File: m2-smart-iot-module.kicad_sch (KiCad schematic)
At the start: 3 parts

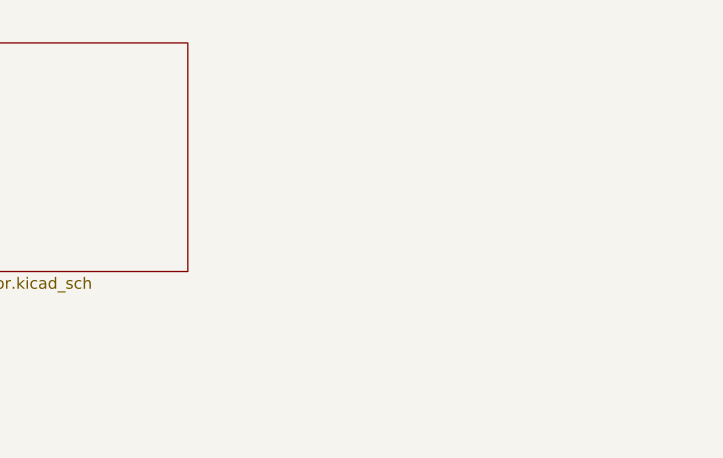
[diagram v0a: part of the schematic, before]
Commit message: Added FTDI schematic
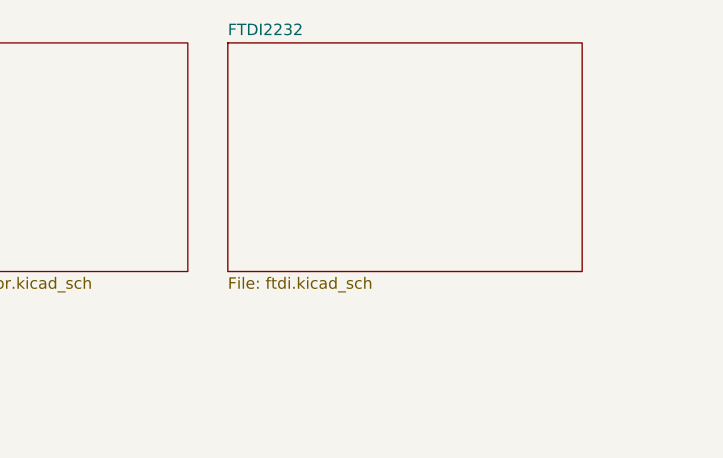
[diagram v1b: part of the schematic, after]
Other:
- added sheet FTDI2232 (ftdi.kicad_sch)
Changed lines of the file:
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@@
+    )
+  )
+  (sheet (at 328.93 114.3) (size 39.37 25.4) (fields_autoplaced)
+    (stroke (width 0.1524) (type solid) (color 0 0 0 0))
+    (fill (color 0 0 0 0.0000))
+    (property "Sheet name" "FTDI2232" (id 0) (at 328.93 113.5884 0)
+      (effects (font (size 1.27 1.27)) (justify left bottom))
+    )
+    (property "Sheet file" "ftdi.kicad_sch" (id 1) (at 328.93 140.2846 0)
+      (effects (font (size 1.27 1.27)) (justify left top))
     )
   )
@@
     (path "/00000000-0000-0000-0000-0000605233cc" (page "5"))
     (path "/00000000-0000-0000-0000-0000605198ab" (page "6"))
+    (path "/68410b93-aca6-44d3-bd1e-cd427080a29c" (page "7"))
   )
   (symbol_instances
@@
       (reference "#PWR0108") (unit 1) (value "GND") (footprint "")
     )
+    (path "/68410b93-aca6-44d3-bd1e-cd427080a29c/11afe054-5b39-465b-bea7-140a33a54372"
+      (reference "#PWR?") (unit 1) (value "GND") (footprint "")
+    )
+    (path "/68410b93-aca6-44d3-bd1e-cd427080a29c/1e138a19-c9d3-4ce1-abef-10dc6e03d6b0"
+      (reference "#PWR?") (unit 1) (value "GND") (footprint "")
+    )
+    (path "/68410b93-aca6-44d3-bd1e-cd427080a29c/3439d517-461f-421f-a266-6f812446a438"
+      (reference "#PWR?") (unit 1) (value "GND") (footprint "")
+    )
+    (path "/68410b93-aca6-44d3-bd1e-cd427080a29c/34daddf2-4aa9-45c0-a5dd-1378e6b328a3"
+      (reference "#PWR?") (unit 1) (value "GND") (footprint "")
+    )
+    (path "/68410b93-aca6-44d3-bd1e-cd427080a29c/41977174-5359-4b9f-993d-9e04af2325ce"
+      (reference "#PWR?") (unit 1) (value "GND") (footprint "")
+    )
+    (path "/68410b93-aca6-44d3-bd1e-cd427080a29c/5dd26dfc-010f-4b59-98a9-fc53bac77c22"
+      (reference "#PWR?") (unit 1) (value "GND") (footprint "")
+    )
+    (path "/68410b93-aca6-44d3-bd1e-cd427080a29c/81cfe2dd-64d2-49dc-92f1-faef74ed356b"
+      (reference "#PWR?") (unit 1) (value "GND") (footprint "")
+    )
+    (path "/68410b93-aca6-44d3-bd1e-cd427080a29c/852b28f0-6b74-43e6-8ae5-e14a61a04115"
+      (reference "#PWR?") (unit 1) (value "GND") (footprint "")
+    )
+    (path "/68410b93-aca6-44d3-bd1e-cd427080a29c/b1091a6c-2627-4ea9-977d-a02c6e01983d"
+      (reference "#PWR?") (unit 1) (value "GND") (footprint "")
+    )
+    (path "/68410b93-aca6-44d3-bd1e-cd427080a29c/b24ad7d7-7447-4ac2-a396-7e9974858242"
+      (reference "#PWR?") (unit 1) (value "GND") (footprint "")
+    )
+    (path "/68410b93-aca6-44d3-bd1e-cd427080a29c/e0a02e44-9724-4dcf-a201-9611e14adbdf"
+      (reference "#PWR?") (unit 1) (value "GND") (footprint "")
+    )
+    (path "/68410b93-aca6-44d3-bd1e-cd427080a29c/e6cb064a-7148-4e0a-bbed-942b0b8c1538"
+      (reference "#PWR?") (unit 1) (value "GND") (footprint "")
+    )
     (path "/00000000-0000-0000-0000-000060519809/00000000-0000-0000-0000-00006053cae5"
       (reference "ANT1") (unit 1) (value "ANT-2.45-CHP-T") (footprint "m2-smart-iot-module-footprints:Linx-ANT-2.45-CHP-T-MFG")
@@
       (reference "C77") (unit 1) (value "C_100n_0402") (footprint "m2-smart-iot-module-footprints:0402-cap")
     )
+    (path "/68410b93-aca6-44d3-bd1e-cd427080a29c/00128c11-9ae6-4452-9d40-6eed6ed4fa92"
+      (reference "C?") (unit 1) (value "C_100n_0402") (footprint "antmicro-footprints:0402-cap")
+    )
+    (path "/68410b93-aca6-44d3-bd1e-cd427080a29c/0683ecee-ab3f-4084-b163-cb6e41987b93"
+      (reference "C?") (unit 1) (value "C_100n_0402") (footprint "antmicro-footprints:0402-cap")
+    )
+    (path "/68410b93-aca6-44d3-bd1e-cd427080a29c/07656054-dac2-43ac-a0ba-60cc3622062b"
+      (reference "C?") (unit 1) (value "C_100n_0402") (footprint "antmicro-footprints:0402-cap")
+    )
+    (path "/68410b93-aca6-44d3-bd1e-cd427080a29c/1f05b071-c8f4-4c21-8c00-c3d2755cccf7"
+      (reference "C?") (unit 1) (value "C_100n_0402") (footprint "antmicro-footprints:0402-cap")
+    )
+    (path "/68410b93-aca6-44d3-bd1e-cd427080a29c/2d7a560d-7fde-4b37-b777-8fd058908345"
+      (reference "C?") (unit 1) (value "C_100n_0402") (footprint "antmicro-footprints:0402-cap")
+    )
+    (path "/68410b93-aca6-44d3-bd1e-cd427080a29c/315f3ffb-9d51-441d-9c46-0e9b7750238d"
+      (reference "C?") (unit 1) (value "C_18p_0402") (footprint "antmicro-footprints:0402-cap")
+    )
+    (path "/68410b93-aca6-44d3-bd1e-cd427080a29c/4143701c-d634-41bd-a301-0c60c388ad5f"
+      (reference "C?") (unit 1) (value "C_100n_0402") (footprint "antmicro-footprints:0402-cap")
+    )
+    (path "/68410b93-aca6-44d3-bd1e-cd427080a29c/73c959b5-8152-4fad-9ade-293313183a87"
+      (reference "C?") (unit 1) (value "C_18p_0402") (footprint "antmicro-footprints:0402-cap")
+    )
+    (path "/68410b93-aca6-44d3-bd1e-cd427080a29c/add7447d-93c8-4ac2-acdb-bb2a61238b8f"
+      (reference "C?") (unit 1) (value "C_10u_0805") (footprint "m2-smart-iot-module-footprints:0805-cap")
+    )
+    (path "/68410b93-aca6-44d3-bd1e-cd427080a29c/e69a35cc-c2a3-403f-b7de-acd2c8207974"
+      (reference "C?") (unit 1) (value "C_100n_0402") (footprint "antmicro-footprints:0402-cap")
+    )
     (path "/00000000-0000-0000-0000-000060519809/00000000-0000-0000-0000-0000623b8f1e"
       (reference "D1") (unit 1) (value "KP-1608CGCK") (footprint "m2-smart-iot-module-footprints:LED0603")
@@
       (reference "FB1") (unit 1) (value "BLM21PG600SN") (footprint "m2-smart-iot-module-footprints:0805-res")
     )
+    (path "/68410b93-aca6-44d3-bd1e-cd427080a29c/1ba44061-29ba-43cb-9cde-cc3db1725136"
+      (reference "FB?") (unit 1) (value "BLM21PG600SN") (footprint "m2-smart-iot-module-footprints:0805-res")
+    )
     (path "/00000000-0000-0000-0000-0000604cff57/659b3f22-a9f3-4d19-b979-88ffbed06828"
       (reference "IC1") (unit 1) (value "UPD720201K8-711-BAC-A") (footprint "antmicro-footprints:QFN40P800X800X90-69N-D")
@@
       (reference "R52") (unit 1) (value "R_0R_0402") (footprint "antmicro-footprints:0402-res")
     )
+    (path "/00000000-0000-0000-0000-0000605233cc/071ba9ef-8d4a-4032-8611-9e9457c33aa7"
+      (reference "R?") (unit 1) (value "R_1k_0402") (footprint "antmicro-footprints:0402-res")
+    )
+    (path "/68410b93-aca6-44d3-bd1e-cd427080a29c/22e4935e-cfb3-465f-b2e5-6b3ebcec47e9"
+      (reference "R?") (unit 1) (value "R_10k_0402") (footprint "antmicro-footprints:0402-res")
+    )
+    (path "/00000000-0000-0000-0000-000060519809/357517c7-91f3-4445-89df-5a4994fd51bb"
+      (reference "R?") (unit 1) (value "R_1k_0402") (footprint "antmicro-footprints:0402-res")
+    )
+    (path "/68410b93-aca6-44d3-bd1e-cd427080a29c/4691fe08-6cea-4c9e-9cc2-3894d30e602d"
+      (reference "R?") (unit 1) (value "R_10k_0402") (footprint "antmicro-footprints:0402-res")
+    )
+    (path "/68410b93-aca6-44d3-bd1e-cd427080a29c/5c795cc7-77ec-4acc-9612-76929e97dfd9"
+      (reference "R?") (unit 1) (value "R_2k2_0402") (footprint "antmicro-footprints:0402-res")
+    )
+    (path "/68410b93-aca6-44d3-bd1e-cd427080a29c/85e35e99-01ee-4c85-a0e8-9b9263b7c426"
+      (reference "R?") (unit 1) (value "R_10k_0402") (footprint "antmicro-footprints:0402-res")
+    )
+    (path "/68410b93-aca6-44d3-bd1e-cd427080a29c/a49e9949-2706-459a-b507-cea25a41afde"
+      (reference "R?") (unit 1) (value "R_12k_0402") (footprint "antmicro-footprints:0402-res")
+    )
+    (path "/68410b93-aca6-44d3-bd1e-cd427080a29c/e29c8173-da2a-43c0-8ce3-638aaee3ba36"
+      (reference "R?") (unit 1) (value "R_10k_0402") (footprint "antmicro-footprints:0402-res")
+    )
     (path "/00000000-0000-0000-0000-000060519809/00000000-0000-0000-0000-00006094bf1c"
       (reference "SW1") (unit 1) (value "PTS840_GK_SMTR_LFS") (footprint "m2-smart-iot-module-footprints:CK-PTS840_GK_SMTR_LFS-0")
@@
       (reference "TP28") (unit 1) (value "TP_SMD1MM") (footprint "m2-smart-iot-module-footprints:Testpoint_smd_1mm")
     )
+    (path "/68410b93-aca6-44d3-bd1e-cd427080a29c/3f5a84f7-9e18-4808-aab2-0e69509107a0"
+      (reference "U1") (unit 1) (value "FT2232H-56Q") (footprint "antmicro-footprints:QFN-56-1EP_8x8mm_P0.5mm_EP5.5.9x5.9mm")
+    )
     (path "/00000000-0000-0000-0000-0000604cff57/00000000-0000-0000-0000-0000604de031"
       (reference "U2") (unit 1) (value "SST25VF512A") (footprint "m2-smart-iot-module-footprints:SOIC8-SST25VF512A-33-4I-SAE-Level_B")
@@
       (reference "U10") (unit 1) (value "MIC2877-5.0YFT-TR") (footprint "m2-smart-iot-module-footprints:FTQFN")
     )
+    (path "/68410b93-aca6-44d3-bd1e-cd427080a29c/d41af900-20ce-4a2e-b28a-32b01b68e5cf"
+      (reference "U?") (unit 1) (value "93LC56CT-IMC") (footprint "antmicro-footprints:DFN-8_2x3mm")
+    )
     (path "/00000000-0000-0000-0000-0000604cff57/00000000-0000-0000-0000-00006060e650"
       (reference "Y1") (unit 1) (value "NX3225SA-24M") (footprint "m2-smart-iot-module-footprints:NDK-NX3225SA-0-0-MFG")
@@
       (reference "Y3") (unit 1) (value "ABS06-32.768KHZ-9-1-T") (footprint "m2-smart-iot-module-footprints:Abracon-ABS06-32.768KHZ-T-0")
     )
+    (path "/68410b93-aca6-44d3-bd1e-cd427080a29c/af6ea41f-d80e-49de-a9b5-51d22eadba5d"
+      (reference "Y?") (unit 1) (value "ABM8G-12M-18-D2Y-T") (footprint "antmicro-footprints:KX-7")
+    )
   )

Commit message: Bumped version to 1.2.2
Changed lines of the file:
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@@
     (title "M.2 Smart IoT Module")
     (date "2022-07-11")
-    (rev "1.2.1")
+    (rev "1.2.2")
     (comment 1 "www.antmicro.com")
     (comment 2 "Antmicro Ltd.")
@@
     )
   )
-  (sheet (at 158.75 114.3) (size 38.1 25.4) (fields_autoplaced)
+  (sheet (at 125.095 114.3) (size 38.1 25.4) (fields_autoplaced)
     (stroke (width 0) (type solid) (color 0 0 0 0))
     (fill (color 0 0 0 0.0000))
-    (property "Sheet name" "PCIe-USB-Bridge" (id 0) (at 158.75 113.5884 0)
+    (property "Sheet name" "PCIe-USB-Bridge" (id 0) (at 125.095 113.5884 0)
       (effects (font (size 1.27 1.27)) (justify left bottom))
     )
-    (property "Sheet file" "pcie-usb-bridge.kicad_sch" (id 1) (at 158.75 140.2846 0)
+    (property "Sheet file" "pcie-usb-bridge.kicad_sch" (id 1) (at 125.095 140.2846 0)
       (effects (font (size 1.27 1.27)) (justify left top))
     )
   )
-  (sheet (at 116.205 114.3) (size 38.1 25.4) (fields_autoplaced)
+  (sheet (at 82.55 114.3) (size 38.1 25.4) (fields_autoplaced)
     (stroke (width 0) (type solid) (color 0 0 0 0))
     (fill (color 0 0 0 0.0000))
-    (property "Sheet name" "M2-Pins" (id 0) (at 116.205 113.5884 0)
+    (property "Sheet name" "M2-Pins" (id 0) (at 82.55 113.5884 0)
       (effects (font (size 1.27 1.27)) (justify left bottom))
     )
-    (property "Sheet file" "M2-Pins.kicad_sch" (id 1) (at 116.205 140.2846 0)
+    (property "Sheet file" "M2-Pins.kicad_sch" (id 1) (at 82.55 140.2846 0)
       (effects (font (size 1.27 1.27)) (justify left top))
     )
   )
-  (sheet (at 201.295 114.3) (size 38.1 25.4) (fields_autoplaced)
+  (sheet (at 167.64 114.3) (size 38.1 25.4) (fields_autoplaced)
     (stroke (width 0) (type solid) (color 0 0 0 0))
     (fill (color 0 0 0 0.0000))
-    (property "Sheet name" "nRF52840" (id 0) (at 201.295 113.5884 0)
+    (property "Sheet name" "nRF52840" (id 0) (at 167.64 113.5884 0)
       (effects (font (size 1.27 1.27)) (justify left bottom))
     )
-    (property "Sheet file" "nRF52840.kicad_sch" (id 1) (at 201.295 140.2846 0)
+    (property "Sheet file" "nRF52840.kicad_sch" (id 1) (at 167.64 140.2846 0)
       (effects (font (size 1.27 1.27)) (justify left top))
     )
   )
-  (sheet (at 286.385 114.3) (size 38.1 25.4) (fields_autoplaced)
+  (sheet (at 252.73 114.3) (size 38.1 25.4) (fields_autoplaced)
     (stroke (width 0) (type solid) (color 0 0 0 0))
     (fill (color 0 0 0 0.0000))
-    (property "Sheet name" "CoralAccelerator" (id 0) (at 286.385 113.5884 0)
+    (property "Sheet name" "CoralAccelerator" (id 0) (at 252.73 113.5884 0)
       (effects (font (size 1.27 1.27)) (justify left bottom))
     )
-    (property "Sheet file" "coralAccelerator.kicad_sch" (id 1) (at 286.385 140.2846 0)
+    (property "Sheet file" "coralAccelerator.kicad_sch" (id 1) (at 252.73 140.2846 0)
       (effects (font (size 1.27 1.27)) (justify left top))
     )
   )
-  (sheet (at 243.84 114.3) (size 38.1 25.4) (fields_autoplaced)
+  (sheet (at 210.185 114.3) (size 38.1 25.4) (fields_autoplaced)
     (stroke (width 0) (type solid) (color 0 0 0 0))
     (fill (color 0 0 0 0.0000))
-    (property "Sheet name" "powerSupply" (id 0) (at 243.84 113.5884 0)
+    (property "Sheet name" "powerSupply" (id 0) (at 210.185 113.5884 0)
       (effects (font (size 1.27 1.27)) (justify left bottom))
     )
-    (property "Sheet file" "powerSupply.kicad_sch" (id 1) (at 243.84 140.2846 0)
+    (property "Sheet file" "powerSupply.kicad_sch" (id 1) (at 210.185 140.2846 0)
       (effects (font (size 1.27 1.27)) (justify left top))
     )
   )
-  (sheet (at 328.93 114.3) (size 39.37 25.4) (fields_autoplaced)
+  (sheet (at 295.275 114.3) (size 39.37 25.4) (fields_autoplaced)
     (stroke (width 0.1524) (type solid) (color 0 0 0 0))
     (fill (color 0 0 0 0.0000))
-    (property "Sheet name" "FTDI2232" (id 0) (at 328.93 113.5884 0)
+    (property "Sheet name" "FTDI2232" (id 0) (at 295.275 113.5884 0)
       (effects (font (size 1.27 1.27)) (justify left bottom))
     )
-    (property "Sheet file" "ftdi.kicad_sch" (id 1) (at 328.93 140.2846 0)
+    (property "Sheet file" "ftdi.kicad_sch" (id 1) (at 295.275 140.2846 0)
       (effects (font (size 1.27 1.27)) (justify left top))
     )
@@
     )
     (path "/68410b93-aca6-44d3-bd1e-cd427080a29c/67b5efa8-acfa-464a-a779-8cca43e04b2b"
-      (reference "#PWR?") (unit 1) (value "GND") (footprint "")
+      (reference "#PWR0121") (unit 1) (value "GND") (footprint "")
     )
     (path "/00000000-0000-0000-0000-000060519809/00000000-0000-0000-0000-00006053cae5"
@@
     )
     (path "/68410b93-aca6-44d3-bd1e-cd427080a29c/a85bec4d-2623-433c-85a9-154996ebdace"
-      (reference "C?") (unit 1) (value "C_100n_0402") (footprint "antmicro-footprints:0402-cap")
+      (reference "C86") (unit 1) (value "C_100n_0402") (footprint "antmicro-footprints:0402-cap")
     )
     (path "/00000000-0000-0000-0000-000060519809/00000000-0000-0000-0000-0000623b8f1e"
